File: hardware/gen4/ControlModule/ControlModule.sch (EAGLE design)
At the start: 38 parts, among them IC1 XMEGA16A4A

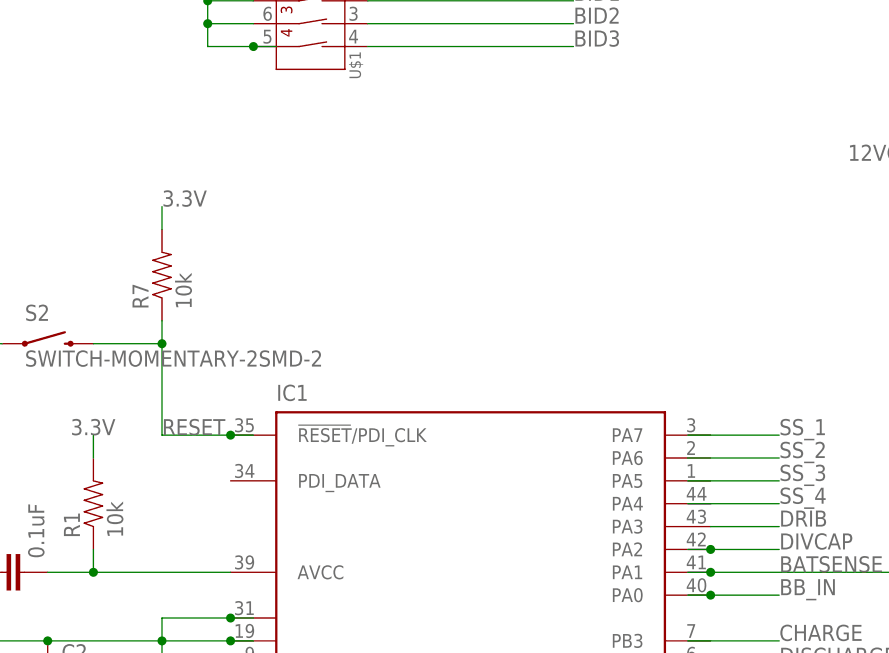
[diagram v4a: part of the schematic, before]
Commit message: Added programmer connector. Microboard should be all set
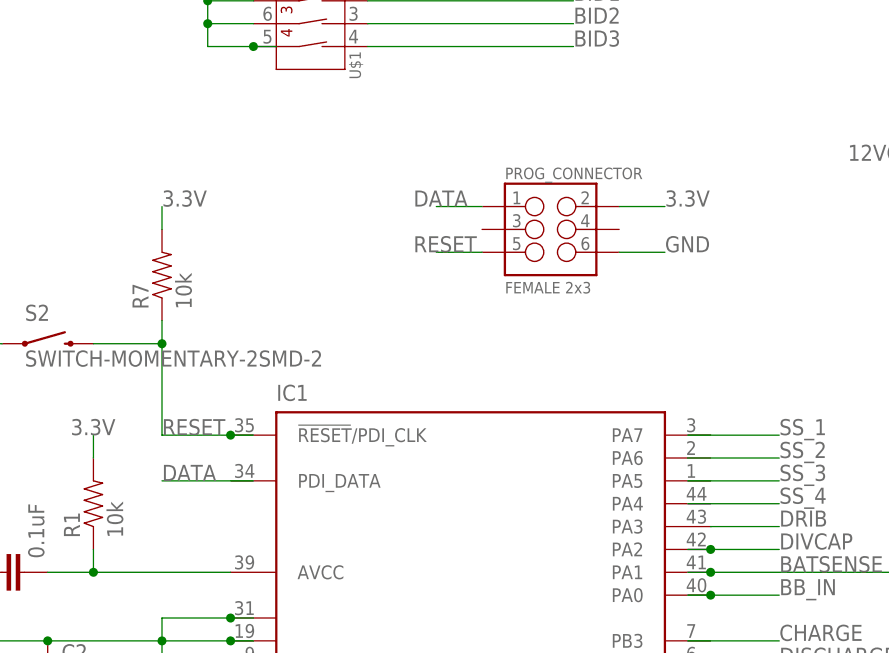
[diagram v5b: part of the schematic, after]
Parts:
- added PROG_CONNECTOR: FEMALE 2x3, SparkFun-Connectors:M03X2FEMALE
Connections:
- new net DATA: PROG_CONNECTOR.1
- net 3.3V: now also PROG_CONNECTOR.2
- net GND: now also PROG_CONNECTOR.6
- net RESET: now also PROG_CONNECTOR.5
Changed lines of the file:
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@@
 <part name="LED3" library="SparkFun-LED" deviceset="LED" device="1206"/>
 <part name="IMU" library="gen3" deviceset="MPU6050IMU" device="MPU"/>
+<part name="PROG_CONNECTOR" library="SparkFun-Connectors" deviceset="M03X2" device="FEMALE" value="FEMALE 2x3"/>
 </parts>
 <sheets>
@@
 <instance part="LED3" gate="G$1" x="226.06" y="119.38"/>
 <instance part="IMU" gate="G$1" x="220.98" y="167.64"/>
+<instance part="PROG_CONNECTOR" gate="G$1" x="83.82" y="114.3"/>
 </instances>
 <busses>
@@
 <pinref part="S2" gate="G$1" pin="2"/>
 <pinref part="R7" gate="G$1" pin="1"/>
+</segment>
+<segment>
+<pinref part="PROG_CONNECTOR" gate="G$1" pin="5"/>
+<wire x1="76.2" y1="111.76" x2="71.12" y2="111.76" width="0.1524" layer="91"/>
+<label x="68.58" y="111.76" size="1.778" layer="95"/>
 </segment>
 </net>
@@
 <wire x1="213.36" y1="170.18" x2="205.74" y2="170.18" width="0.1524" layer="91"/>
 <label x="203.2" y="170.18" size="1.778" layer="95"/>
+</segment>
+<segment>
+<pinref part="PROG_CONNECTOR" gate="G$1" pin="6"/>
+<wire x1="91.44" y1="111.76" x2="96.52" y2="111.76" width="0.1524" layer="91"/>
+<label x="96.52" y="111.76" size="1.778" layer="95"/>
 </segment>
 </net>
@@
 <label x="203.2" y="172.72" size="1.778" layer="95"/>
 </segment>
+<segment>
+<pinref part="PROG_CONNECTOR" gate="G$1" pin="2"/>
+<wire x1="91.44" y1="116.84" x2="96.52" y2="116.84" width="0.1524" layer="91"/>
+<label x="96.52" y="116.84" size="1.778" layer="95"/>
+</segment>
 </net>
 <net name="N$1" class="0">
@@
 </segment>
 </net>
+<net name="DATA" class="0">
+<segment>
+<pinref part="PROG_CONNECTOR" gate="G$1" pin="1"/>
+<wire x1="76.2" y1="116.84" x2="71.12" y2="116.84" width="0.1524" layer="91"/>
+<label x="68.58" y="116.84" size="1.778" layer="95"/>
+</segment>
+<segment>
+<wire x1="50.8" y1="86.36" x2="40.64" y2="86.36" width="0.1524" layer="91"/>
+<label x="40.64" y="86.36" size="1.778" layer="95"/>
+</segment>
+</net>

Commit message: Initial layout of microboard
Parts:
- R2, R3, R4: value (none) -> 4.7k
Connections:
- new net CHARGE: IC1.PB3, KICKER_HEADER.1
- new net CHIP_ENABLE: IC1.PC3, KICKER_HEADER.4
- new net KICK_ENABLE: IC1.PC4, KICKER_HEADER.5
- new net SS_1: IC1.PA7, SPI_HEADER.4
- new net SS_2: IC1.PA6, SPI_HEADER.5, SPI_HEADER.6
- new net SS_3: IC1.PA5, SPI_HEADER.7
- new net SS_4: IC1.PA4, SPI_HEADER.8
- net BB_IN: now also KICKER_HEADER.10
- net BB_OUT: now also KICKER_HEADER.8
- net CTS: now also IC1.PD4
- net DATA: now also IC1.PDI_DATA
- net DISCHARGE: now also IC1.PB2
- net DIVCAP: now also KICKER_HEADER.9
- net DONE: now also KICKER_HEADER.3
- net DRIB: now also KICKER_HEADER.6
- net GLED1: now also IC1.PR0(XT2)
- net INT: now also IC1.PC2
- net KICK_REF: now also KICKER_HEADER.7
- net N$6: now also SPI_HEADER.1
- net N$7: now also SPI_HEADER.2
- net N$8: now also SPI_HEADER.3
- net RLED1: now also IC1.PR1(XT1)
- net RTS: now also IC1.PD5
- net RX: now also IC1.PD6
- net SCL: now also IC1.PC1
- net SDA: now also IC1.PC0
- net TX: now also IC1.PD7

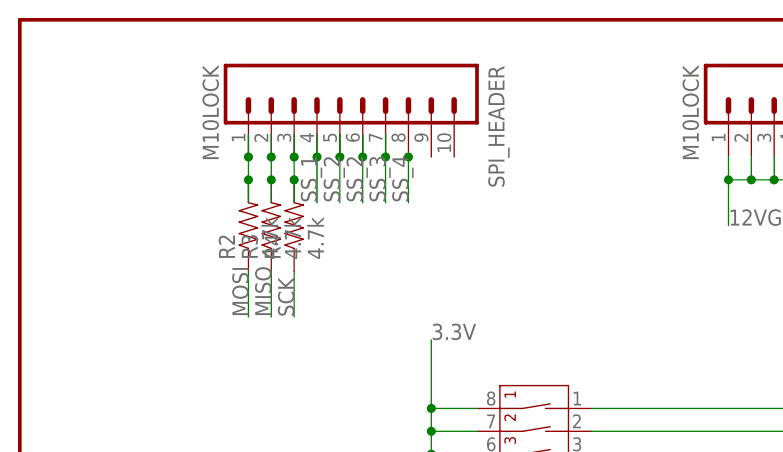
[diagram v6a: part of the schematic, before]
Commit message: Improved commsboard layout
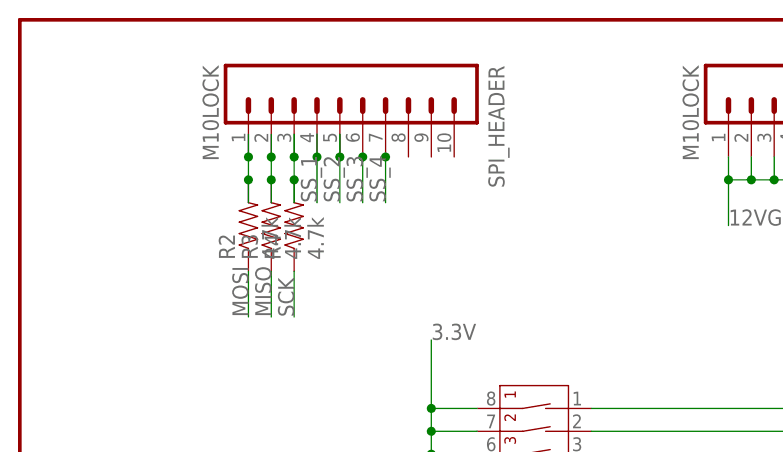
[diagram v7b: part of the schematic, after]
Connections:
- net SS_2: no longer SPI_HEADER.6
- net SS_3: now also SPI_HEADER.6; no longer SPI_HEADER.7
- net SS_4: now also SPI_HEADER.7; no longer SPI_HEADER.8
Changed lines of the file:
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@@
 <wire x1="35.56" y1="170.18" x2="35.56" y2="165.1" width="0.1524" layer="91"/>
-</segment>
-<segment>
-<wire x1="38.1" y1="172.72" x2="38.1" y2="170.18" width="0.1524" layer="91"/>
-<label x="38.1" y="165.1" size="1.778" layer="95" rot="R90"/>
-<pinref part="SPI_HEADER" gate="G$1" pin="6"/>
-<junction x="38.1" y="170.18"/>
-<wire x1="38.1" y1="170.18" x2="38.1" y2="165.1" width="0.1524" layer="91"/>
 </segment>
 </net>
@@
 </segment>
 <segment>
-<wire x1="40.64" y1="172.72" x2="40.64" y2="170.18" width="0.1524" layer="91"/>
-<label x="40.64" y="165.1" size="1.778" layer="95" rot="R90"/>
-<pinref part="SPI_HEADER" gate="G$1" pin="7"/>
-<junction x="40.64" y="170.18"/>
-<wire x1="40.64" y1="170.18" x2="40.64" y2="165.1" width="0.1524" layer="91"/>
+<pinref part="SPI_HEADER" gate="G$1" pin="6"/>
+<wire x1="38.1" y1="170.18" x2="38.1" y2="165.1" width="0.1524" layer="91"/>
+<junction x="38.1" y="170.18"/>
+<label x="38.1" y="165.1" size="1.778" layer="95" rot="R90"/>
 </segment>
 </net>
@@
 </segment>
 <segment>
-<pinref part="SPI_HEADER" gate="G$1" pin="8"/>
-<wire x1="43.18" y1="170.18" x2="43.18" y2="165.1" width="0.1524" layer="91"/>
-<junction x="43.18" y="170.18"/>
-<label x="43.18" y="165.1" size="1.778" layer="95" rot="R90"/>
-</segment>
-</net>
+<pinref part="SPI_HEADER" gate="G$1" pin="7"/>
+<wire x1="40.64" y1="170.18" x2="40.64" y2="165.1" width="0.1524" layer="91"/>
+<junction x="40.64" y="170.18"/>
+<label x="40.64" y="165.1" size="1.778" layer="95" rot="R90"/>
+</segment>
+</net>

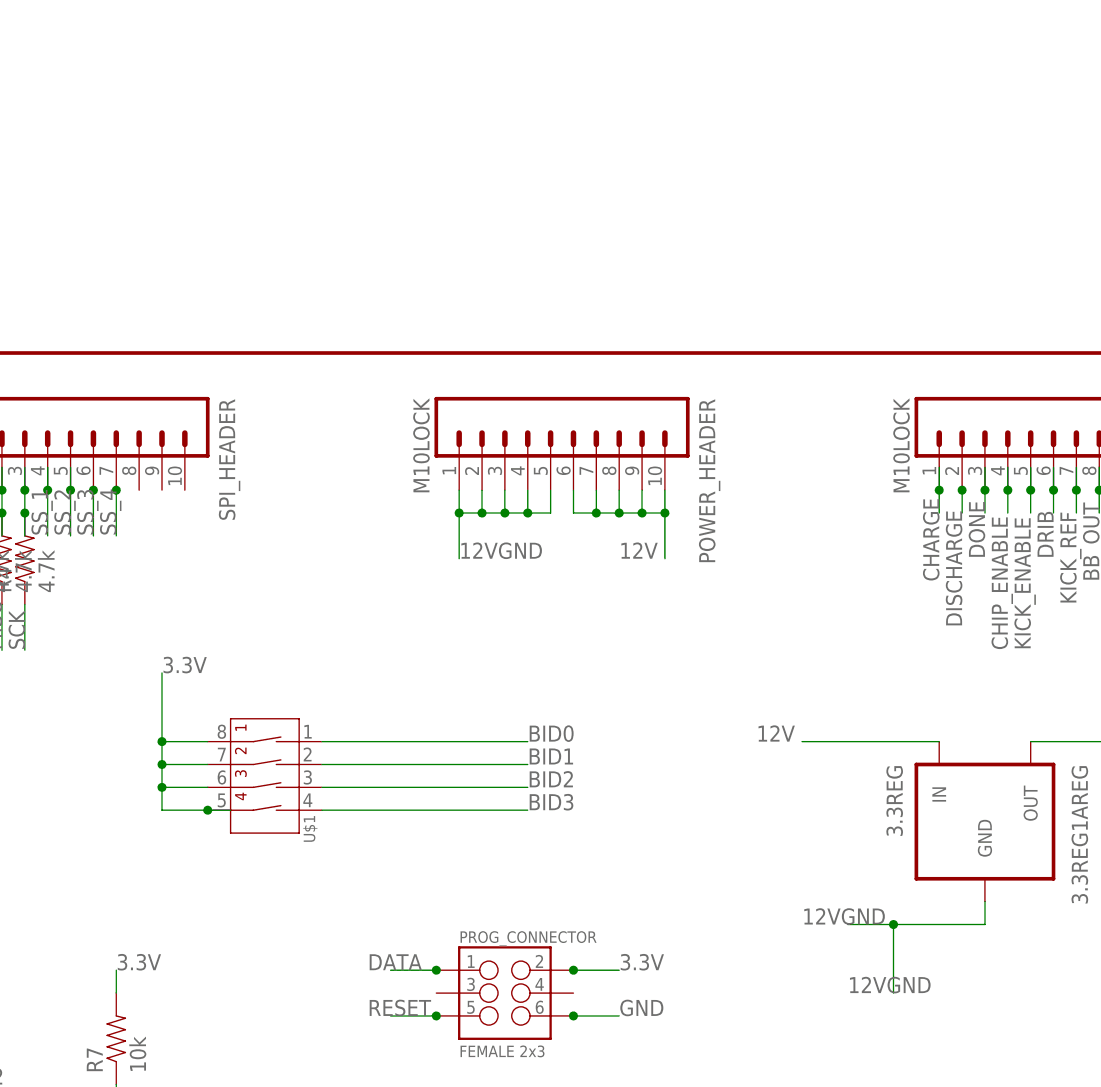
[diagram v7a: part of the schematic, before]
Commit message: control board fixes
Pull up changed, connector added
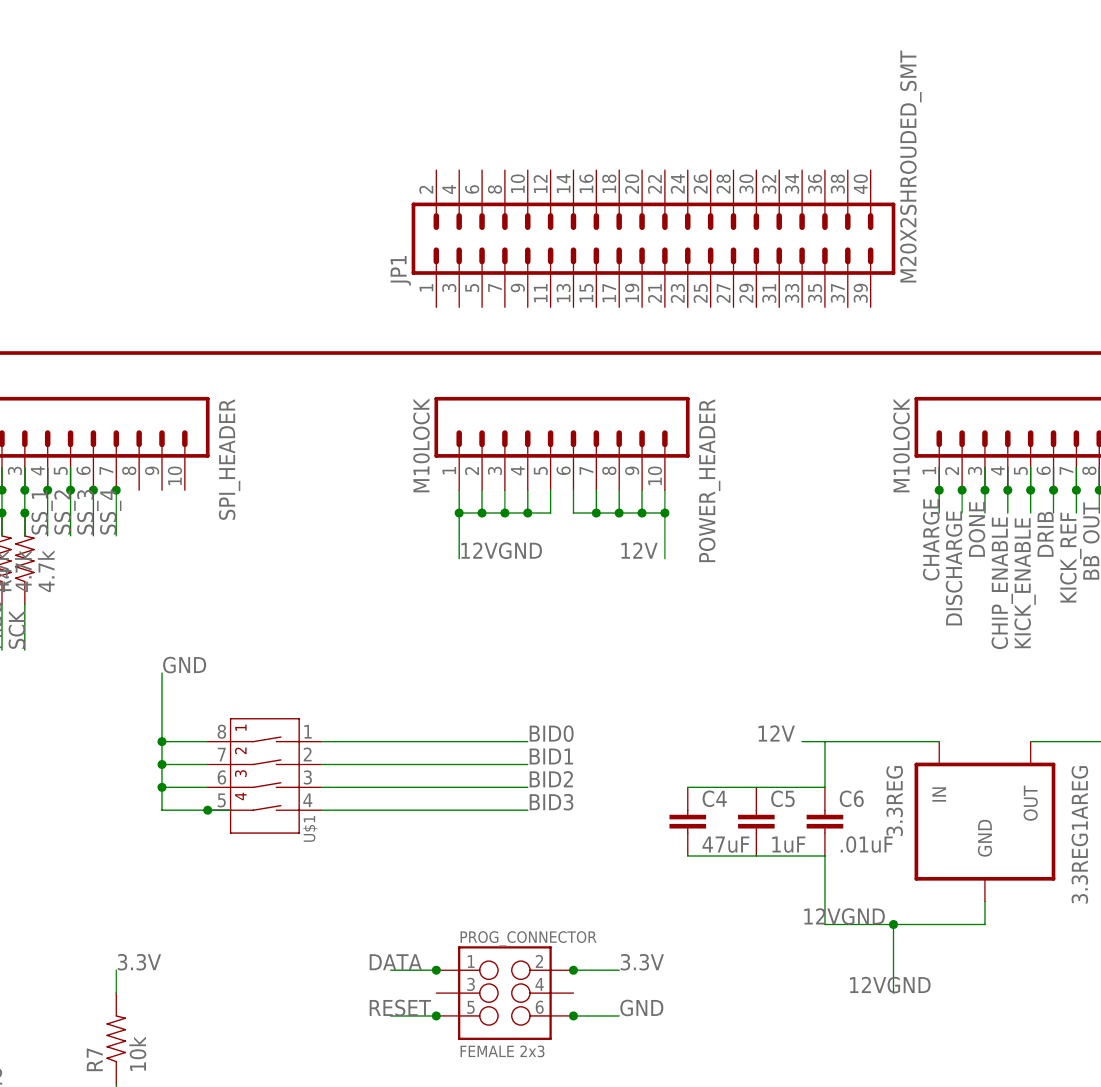
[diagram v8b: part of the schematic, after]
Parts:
- added C4: 47uF, SparkFun-Capacitors:CAP1206
- added C5: 1uF, SparkFun-Capacitors:CAP0805
- added C6: .01uF, SparkFun-Capacitors:CAP0805
- added JP1: M20X2SHROUDED_SMT, SparkFun-Connectors:M20X2SHROUDED_SMT
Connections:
- net 12V: now also C4.1, C5.1, C6.1
- net 12VGND: now also C4.2, C5.2, C6.2
- net 3.3V: no longer U$1.1B, U$1.2B, U$1.3B, U$1.4B
- net GND: now also U$1.1B, U$1.2B, U$1.3B, U$1.4B
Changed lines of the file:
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@@
 <layers>
 <layer number="1" name="Top" color="4" fill="1" visible="no" active="no"/>
+<layer number="2" name="Route2" color="1" fill="3" visible="no" active="no"/>
+<layer number="3" name="Route3" color="4" fill="3" visible="no" active="no"/>
+<layer number="4" name="Route4" color="1" fill="4" visible="no" active="no"/>
+<layer number="5" name="Route5" color="4" fill="4" visible="no" active="no"/>
+<layer number="6" name="Route6" color="1" fill="8" visible="no" active="no"/>
+<layer number="7" name="Route7" color="4" fill="8" visible="no" active="no"/>
+<layer number="8" name="Route8" color="1" fill="2" visible="no" active="no"/>
+<layer number="9" name="Route9" color="4" fill="2" visible="no" active="no"/>
+<layer number="10" name="Route10" color="1" fill="7" visible="no" active="no"/>
+<layer number="11" name="Route11" color="4" fill="7" visible="no" active="no"/>
+<layer number="12" name="Route12" color="1" fill="5" visible="no" active="no"/>
+<layer number="13" name="Route13" color="4" fill="5" visible="no" active="no"/>
+<layer number="14" name="Route14" color="1" fill="6" visible="no" active="no"/>
+<layer number="15" name="Route15" color="4" fill="6" visible="no" active="no"/>
 <layer number="16" name="Bottom" color="1" fill="1" visible="no" active="no"/>
 <layer number="17" name="Pads" color="2" fill="1" visible="no" active="no"/>
@@
 <layer number="112" name="tSilk" color="7" fill="1" visible="no" active="yes"/>
 <layer number="113" name="IDFDebug" color="4" fill="1" visible="no" active="yes"/>
+<layer number="114" name="Badge_Outline" color="7" fill="1" visible="yes" active="yes"/>
+<layer number="115" name="ReferenceISLANDS" color="7" fill="1" visible="yes" active="yes"/>
 <layer number="116" name="Patch_BOT" color="9" fill="4" visible="yes" active="yes"/>
+<layer number="118" name="Rect_Pads" color="7" fill="1" visible="yes" active="yes"/>
 <layer number="121" name="_tsilk" color="7" fill="1" visible="yes" active="yes"/>
 <layer number="122" name="_bsilk" color="7" fill="1" visible="yes" active="yes"/>
@@
 <part name="IMU" library="gen3" deviceset="MPU6050IMU" device="MPU"/>
 <part name="PROG_CONNECTOR" library="SparkFun-Connectors" deviceset="M03X2" device="FEMALE" value="FEMALE 2x3"/>
+<part name="C4" library="SparkFun-Capacitors" deviceset="CAP" device="1206" value="47uF"/>
+<part name="C5" library="SparkFun-Capacitors" deviceset="CAP" device="0805" value="1uF"/>
+<part name="C6" library="SparkFun-Capacitors" deviceset="CAP" device="0805" value=".01uF"/>
+<part name="JP1" library="SparkFun-Connectors" deviceset="M20X2" device="SHROUDED_SMT"/>
 </parts>
 <sheets>
@@
 <instance part="IMU" gate="G$1" x="220.98" y="167.64"/>
 <instance part="PROG_CONNECTOR" gate="G$1" x="83.82" y="114.3"/>
+<instance part="C4" gate="G$1" x="104.14" y="132.08"/>
+<instance part="C5" gate="G$1" x="111.76" y="132.08"/>
+<instance part="C6" gate="G$1" x="119.38" y="132.08"/>
+<instance part="JP1" gate="G$1" x="99.06" y="198.12" rot="R90"/>
 </instances>
 <busses>
@@
 <label x="96.52" y="111.76" size="1.778" layer="95"/>
 <junction x="91.44" y="111.76"/>
+</segment>
+<segment>
+<pinref part="U$1" gate="G$1" pin="1B"/>
+<wire x1="50.8" y1="142.24" x2="45.72" y2="142.24" width="0.1524" layer="91"/>
+<pinref part="U$1" gate="G$1" pin="2B"/>
+<wire x1="50.8" y1="139.7" x2="45.72" y2="139.7" width="0.1524" layer="91"/>
+<wire x1="45.72" y1="139.7" x2="45.72" y2="142.24" width="0.1524" layer="91"/>
+<pinref part="U$1" gate="G$1" pin="3B"/>
+<wire x1="50.8" y1="137.16" x2="45.72" y2="137.16" width="0.1524" layer="91"/>
+<wire x1="45.72" y1="137.16" x2="45.72" y2="139.7" width="0.1524" layer="91"/>
+<junction x="45.72" y="139.7"/>
+<wire x1="53.34" y1="134.62" x2="50.8" y2="134.62" width="0.1524" layer="91"/>
+<wire x1="50.8" y1="134.62" x2="45.72" y2="134.62" width="0.1524" layer="91"/>
+<wire x1="45.72" y1="134.62" x2="45.72" y2="137.16" width="0.1524" layer="91"/>
+<junction x="45.72" y="137.16"/>
+<wire x1="45.72" y1="142.24" x2="45.72" y2="149.86" width="0.1524" layer="91"/>
+<junction x="45.72" y="142.24"/>
+<label x="45.72" y="149.86" size="1.778" layer="95"/>
+<pinref part="U$1" gate="G$1" pin="4B"/>
+<junction x="50.8" y="134.62"/>
 </segment>
 </net>
@@
 </segment>
 <segment>
-<pinref part="U$1" gate="G$1" pin="1B"/>
-<wire x1="50.8" y1="142.24" x2="45.72" y2="142.24" width="0.1524" layer="91"/>
-<pinref part="U$1" gate="G$1" pin="2B"/>
-<wire x1="50.8" y1="139.7" x2="45.72" y2="139.7" width="0.1524" layer="91"/>
-<wire x1="45.72" y1="139.7" x2="45.72" y2="142.24" width="0.1524" layer="91"/>
-<pinref part="U$1" gate="G$1" pin="3B"/>
-<wire x1="50.8" y1="137.16" x2="45.72" y2="137.16" width="0.1524" layer="91"/>
-<wire x1="45.72" y1="137.16" x2="45.72" y2="139.7" width="0.1524" layer="91"/>
-<junction x="45.72" y="139.7"/>
-<wire x1="53.34" y1="134.62" x2="50.8" y2="134.62" width="0.1524" layer="91"/>
-<wire x1="50.8" y1="134.62" x2="45.72" y2="134.62" width="0.1524" layer="91"/>
-<wire x1="45.72" y1="134.62" x2="45.72" y2="137.16" width="0.1524" layer="91"/>
-<junction x="45.72" y="137.16"/>
-<wire x1="45.72" y1="142.24" x2="45.72" y2="149.86" width="0.1524" layer="91"/>
-<junction x="45.72" y="142.24"/>
-<label x="45.72" y="149.86" size="1.778" layer="95"/>
-<pinref part="U$1" gate="G$1" pin="4B"/>
-<junction x="50.8" y="134.62"/>
-</segment>
-<segment>
 <pinref part="XBEE" gate="G$1" pin="VDD"/>
 <wire x1="180.34" y1="71.12" x2="172.72" y2="71.12" width="0.1524" layer="91"/>
@@
 <segment>
 <pinref part="3.3REG" gate="G$1" pin="IN"/>
-<wire x1="116.84" y1="142.24" x2="132.08" y2="142.24" width="0.1524" layer="91"/>
+<wire x1="116.84" y1="142.24" x2="119.38" y2="142.24" width="0.1524" layer="91"/>
 <label x="111.76" y="142.24" size="1.778" layer="95"/>
+<pinref part="C4" gate="G$1" pin="1"/>
+<pinref part="C5" gate="G$1" pin="1"/>
+<wire x1="119.38" y1="142.24" x2="132.08" y2="142.24" width="0.1524" layer="91"/>
+<wire x1="104.14" y1="137.16" x2="111.76" y2="137.16" width="0.1524" layer="91"/>
+<pinref part="C6" gate="G$1" pin="1"/>
+<wire x1="111.76" y1="137.16" x2="119.38" y2="137.16" width="0.1524" layer="91"/>
+<wire x1="119.38" y1="137.16" x2="119.38" y2="142.24" width="0.1524" layer="91"/>
 </segment>
 <segment>
@@
 <segment>
 <pinref part="3.3REG" gate="G$1" pin="GND"/>
-<wire x1="121.92" y1="121.92" x2="127" y2="121.92" width="0.1524" layer="91"/>
 <wire x1="127" y1="121.92" x2="137.16" y2="121.92" width="0.1524" layer="91"/>
 <wire x1="137.16" y1="121.92" x2="137.16" y2="124.46" width="0.1524" layer="91"/>
@@
 <junction x="127" y="121.92"/>
 <label x="121.92" y="114.3" size="1.778" layer="95"/>
-</segment>
-<segment>
+<pinref part="C6" gate="G$1" pin="2"/>
+<wire x1="127" y1="121.92" x2="119.38" y2="121.92" width="0.1524" layer="91"/>
+<wire x1="119.38" y1="121.92" x2="119.38" y2="129.54" width="0.1524" layer="91"/>
+<pinref part="C5" gate="G$1" pin="2"/>
+<wire x1="119.38" y1="129.54" x2="111.76" y2="129.54" width="0.1524" layer="91"/>
+<pinref part="C4" gate="G$1" pin="2"/>
+<wire x1="111.76" y1="129.54" x2="104.14" y2="129.54" width="0.1524" layer="91"/>
+</segment>
+<segment>
